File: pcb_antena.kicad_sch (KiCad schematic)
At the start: 29 parts, among them J1 Screw_Terminal_01x02, J2 Screw_Terminal_01x02, J3 Screw_Terminal_01x02, U1 TL084, U2 TL082, U3 LM7818_TO220, U4 AD620

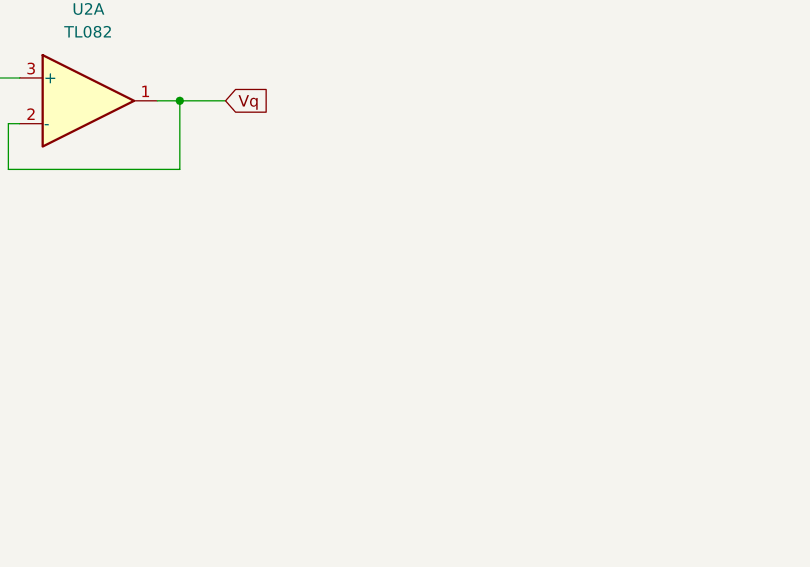
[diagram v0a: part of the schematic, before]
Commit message: Pasaje de componentes y netlist a pcb
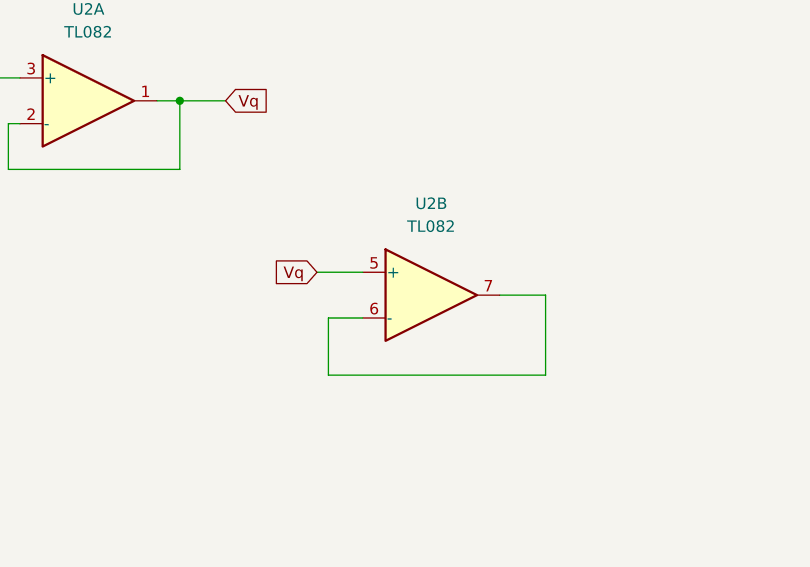
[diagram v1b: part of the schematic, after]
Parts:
- added unit 2 of U2
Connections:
- net Vq: now also U2.5 (+)
- new net: U2.6 (-), U2.7
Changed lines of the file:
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@@
 	(wire
 		(pts
+			(xy 226.06 68.58) (xy 222.25 68.58)
+		)
+		(stroke
+			(width 0)
+			(type default)
+		)
+	)
+	(wire
+		(pts
 			(xy 171.45 39.37) (xy 171.45 41.91)
 		)
@@
 	(wire
 		(pts
+			(xy 222.25 74.93) (xy 246.38 74.93)
+		)
+		(stroke
+			(width 0)
+			(type default)
+		)
+	)
+	(wire
+		(pts
 			(xy 34.29 128.27) (xy 50.8 128.27)
 		)
@@
 	(wire
 		(pts
+			(xy 246.38 74.93) (xy 246.38 66.04)
+		)
+		(stroke
+			(width 0)
+			(type default)
+		)
+	)
+	(wire
+		(pts
 			(xy 222.25 111.76) (xy 229.87 111.76)
 		)
@@
 	(wire
 		(pts
+			(xy 222.25 68.58) (xy 222.25 74.93)
+		)
+		(stroke
+			(width 0)
+			(type default)
+		)
+	)
+	(wire
+		(pts
 			(xy 201.93 128.27) (xy 201.93 116.84)
 		)
@@
 	(wire
 		(pts
+			(xy 246.38 66.04) (xy 241.3 66.04)
+		)
+		(stroke
+			(width 0)
+			(type default)
+		)
+	)
+	(wire
+		(pts
 			(xy 114.3 52.07) (xy 129.54 52.07)
 		)
@@
 		)
 	)
+	(wire
+		(pts
+			(xy 220.98 63.5) (xy 226.06 63.5)
+		)
+		(stroke
+			(width 0)
+			(type default)
+		)
+	)
 	(global_label "Vq"
 		(shape input)
@@
 	(global_label "Vq"
 		(shape input)
+		(at 220.98 63.5 180)
+		(fields_autoplaced yes)
+		(effects
+			(font
+				(size 1.27 1.27)
+			)
+			(justify right)
+		)
+		(property "Intersheetrefs" "${INTERSHEET_REFS}"
+			(at 215.7572 63.5 0)
+			(effects
+				(font
+					(size 1.27 1.27)
+				)
+				(justify right)
+				(hide yes)
+			)
+		)
+	)
+	(global_label "Vq"
+		(shape input)
 		(at 49.53 110.49 180)
 		(fields_autoplaced yes)
@@
 				)
 			)
+		)
+	)
+	(symbol
+		(lib_id "Amplifier_Operational:TL082")
+		(at 233.68 66.04 0)
+		(unit 2)
+		(exclude_from_sim no)
+		(in_bom yes)
+		(on_board yes)
+		(dnp no)
+		(fields_autoplaced yes)
+		(property "Reference" "U2"
+			(at 233.68 55.88 0)
+			(effects
+				(font
+					(size 1.27 1.27)
+				)
+			)
+		)
+		(property "Value" "TL082"
+			(at 233.68 58.42 0)
+			(effects
+				(font
+					(size 1.27 1.27)
+				)
+			)
+		)
+		(property "Footprint" ""
+			(at 233.68 66.04 0)
+			(effects
+				(font
+					(size 1.27 1.27)
+				)
+				(hide yes)
+			)
+		)
+		(property "Datasheet" "http://www.ti.com/lit/ds/symlink/tl081.pdf"
+			(at 233.68 66.04 0)
+			(effects
+				(font
+					(size 1.27 1.27)
+				)
+				(hide yes)
+			)
+		)
+		(property "Description" "Dual JFET-Input Operational Amplifiers, DIP-8/SOIC-8/SSOP-8"
+			(at 233.68 66.04 0)
+			(effects
+				(font
+					(size 1.27 1.27)
+				)
+				(hide yes)
+			)
+		)
+		(pin "2"
+		)
+		(pin "1"
+		)
+		(pin "8"
+		)
+		(pin "6"
+		)
+		(pin "5"
+		)
+		(pin "7"
+		)
+		(pin "4"
+		)
+		(pin "3"
+		)
+		(instances
+			(project ""
+				(path "/d06a90f2-131c-4d35-8833-41ab8319c85a"
+					(reference "U2")
+					(unit 2)
+				)
+			)

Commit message: Versión lista para imprimir
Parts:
- removed J3: Screw_Terminal_01x02, TerminalBlock_MetzConnect:TerminalBlock_MetzConnect_Type011_RT05502HBLC_1x02_P5.00mm_Horizontal, symbol Connector:Screw_Terminal_01x02
- added H1, H2, H3, H4: MountingHole_2.2mm_M2_ISO7380_Pad, MountingHole:MountingHole_2.2mm_M2_ISO7380_Pad, symbol Mechanical:MountingHole_Pad
- added J4: SMA, Connector_Coaxial:SMA_Amphenol_132289_EdgeMount, symbol Connector:Conn_Coaxial_Small
- added R13, R14: 0, huellas_proyecto:R_Axial_DIN0207_L6.3mm_D2.5mm_P10.16mm_Horizontal-pad2mm, symbol Device:R_US
- C1, C5, C6, C9: footprint Capacitor_THT:CP_Radial_D10.0mm_P5.00mm -> huellas_proyecto:CP_Radial_D10.0mm_P5.00mm-pad2mm2
- C2, C3, C4, C7, C8: footprint Capacitor_THT:C_Disc_D5.1mm_W3.2mm_P5.00mm -> huellas_proyecto:C_Disc_D5.1mm_W3.2mm_P5.00mm-pad2mm
- J1: value Screw_Terminal_01x02 -> VC_24V
- J2: value Screw_Terminal_01x02 -> Ant
- R1, R10, R11, R12, R2, R5, R6, R7, R8, R9: footprint Resistor_THT:R_Axial_DIN0207_L6.3mm_D2.5mm_P10.16mm_Horizontal -> huellas_proyecto:R_Axial_DIN0207_L6.3mm_D2.5mm_P10.16mm_Horizontal-pad2mm
- R3, R4: footprint Resistor_THT:R_Axial_DIN0207_L6.3mm_D2.5mm_P10.16mm_Horizontal -> huellas_proyecto:R_Axial_DIN0207_L6.3mm_D2.5mm_P15.24mm_Horizontal-pad2mm
- RV1: footprint Potentiometer_THT:Potentiometer_Bourns_3296W_Vertical -> huellas_proyecto:Potentiometer_Bourns_3296W_Vertical-pad2mm
- U1: footprint Package_DIP:DIP-14_W7.62mm_LongPads -> huellas_proyecto:DIP-14_W7.62mm_LongPads-2mm
- U2, U4: footprint Package_DIP:DIP-8_W7.62mm_LongPads -> huellas_proyecto:DIP-8_W7.62mm_LongPads-pad2mm
- U2: footprint (none) -> huellas_proyecto:DIP-8_W7.62mm_LongPads-pad2mm
- U3: footprint Package_TO_SOT_THT:TO-220-3_Horizontal_TabDown -> huellas_proyecto:TO-220-3_Vertical-pad2mm
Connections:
- net GND: now also J1.2 (Pin_2), H1.1, H2.1, H3.1, H4.1, J4.2 (Ext); no longer J1.1 (Pin_1)
- net at R5.2, R6.2, U1.14: now also R13.1; no longer U1.5 (+)
- net at C1.1, C2.1, U3.1 (VI): now also J1.1 (Pin_1); no longer J1.2 (Pin_2)
- net at C9.2: now also J4.1 (In)
- net at R10.2, R9.2, U1.1: now also R14.1; no longer U1.10 (+)
- net at U1.8, U1.9 (-): now also C7.1; no longer C8.1
- net at U1.6 (-), U1.7: now also C8.1; no longer C7.1
- new net: R13.2, U1.10 (+)
- new net: R14.2, U1.5 (+)
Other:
- moved on the sheet: J1, J2, U1B, U1C

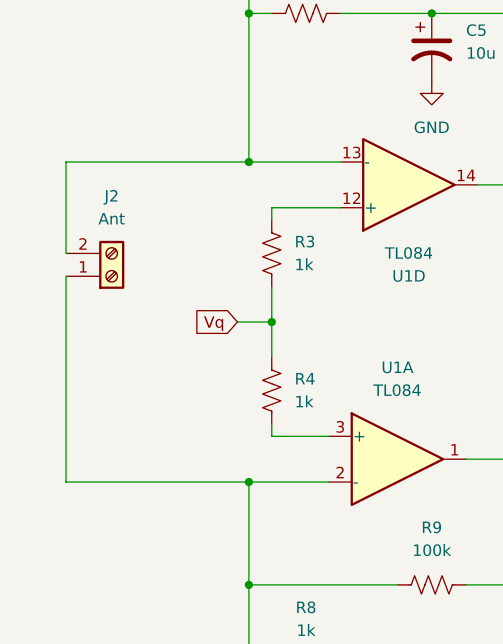
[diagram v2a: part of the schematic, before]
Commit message: Se agrego la otra placa en carpeta una nueva carpeta. Para revisión
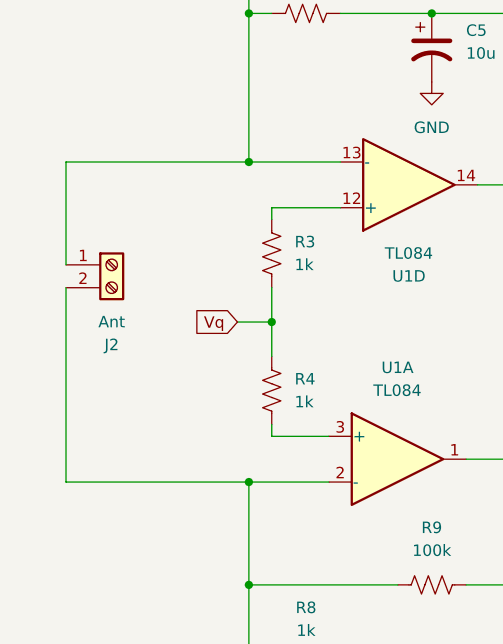
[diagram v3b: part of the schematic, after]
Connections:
- net at R5.1, R7.1, U1.13 (-): now also J2.1 (Pin_1); no longer J2.2 (Pin_2)
- net at R8.1, R9.1, U1.2 (-): now also J2.2 (Pin_2); no longer J2.1 (Pin_1)
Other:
- moved on the sheet: J2
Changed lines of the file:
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@@
-	(wire
-		(pts
-			(xy 30.48 105.41) (xy 30.48 128.27)
-		)
-		(stroke
-			(width 0)
-			(type default)
-		)
-	)
 	(wire
 		(pts
@@
 	(wire
 		(pts
-			(xy 30.48 92.71) (xy 30.48 102.87)
+			(xy 30.48 92.71) (xy 30.48 104.14)
 		)
 		(stroke
@@
 		(pts
 			(xy 205.74 52.07) (xy 205.74 44.45)
+		)
+		(stroke
+			(width 0)
+			(type default)
+		)
+	)
+	(wire
+		(pts
+			(xy 30.48 106.68) (xy 30.48 128.27)
 		)
 		(stroke
@@
 	(symbol
 		(lib_id "Connector:Screw_Terminal_01x02")
-		(at 35.56 105.41 0)
-		(mirror x)
+		(at 35.56 104.14 0)
 		(unit 1)
 		(exclude_from_sim no)
@@
 		(dnp no)
 		(property "Reference" "J2"
-			(at 35.56 96.52 0)
+			(at 35.56 113.03 0)
 			(effects
 				(font
@@
 		)
 		(property "Value" "Ant"
-			(at 35.56 99.06 0)
+			(at 35.56 110.49 0)
 			(effects
 				(font
@@
 		)
 		(property "Footprint" "TerminalBlock_MetzConnect:TerminalBlock_MetzConnect_Type011_RT05502HBLC_1x02_P5.00mm_Horizontal"
-			(at 35.56 105.41 0)
+			(at 35.56 104.14 0)
 			(effects
 				(font
@@
 		)
 		(property "Datasheet" "~"
-			(at 35.56 105.41 0)
+			(at 35.56 104.14 0)
 			(effects
 				(font
@@
 		)
 		(property "Description" "Generic screw terminal, single row, 01x02, script generated (kicad-library-utils/schlib/autogen/connector/)"
-			(at 35.56 105.41 0)
-			(effects
-				(font
+			(at 35.56 104.14 0)
+			(effects
+				(font
